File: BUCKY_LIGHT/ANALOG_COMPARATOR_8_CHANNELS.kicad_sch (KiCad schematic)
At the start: 12 parts, among them IC15 LM319N_NOPB, IC16 LM319N_NOPB, IC17 LM319N_NOPB, IC18 LM319N_NOPB

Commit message: finish up robot (i think)
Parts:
- removed IC15, IC16, IC17, IC18: LM319N_NOPB, DIP794W56P254L1905H533Q14N, symbol ANALOG_COMP:LM319N_NOPB
- removed LI21, LI22, LI24, LI25, LI26, LI27 (x2), LI28: LED, symbol Device:LED
- added IC3, IC4: TLV7034RTER, BUCKY_LIGHT:ANALOG_COMP, symbol ANALOG_COMP:TLV7034RTER
- added LI10, LI11, LI12, LI13, LI14, LI8, LI9: LED, LED_SMD:LED_0603_1608Metric, symbol Device:LED
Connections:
- net +5V: now also IC3.2 (VCC), IC4.2 (VCC)
- net GND: now also IC3.11 (VEE), IC4.11 (VEE)
- net I1: now also IC3.1 (+IN_A)
- net I2: now also IC3.4 (+IN_B)
- net I3: now also IC3.9 (+IN_C)
- net I4: now also IC3.12 (+IN_D)
- net I5: now also IC4.1 (+IN_A)
- net I6: now also IC4.4 (+IN_B)
- net I7: now also IC4.9 (+IN_C)
- new net: IC4.15 (OUT_A), LI12.2 (A)
- new net: IC3.14 (OUT_D), LI11.2 (A)
- new net: IC3.15 (OUT_A), LI8.2 (A)
- new net: IC3.6 (OUT_B), LI9.2 (A)
- new net: IC3.7 (OUT_C), LI10.2 (A)
- new net: IC4.6 (OUT_B), LI13.2 (A)
- new net: IC4.7 (OUT_C), LI14.2 (A)
- new net O: LI10.1 (K), LI11.1 (K), LI12.1 (K), LI13.1 (K), LI14.1 (K), LI8.1 (K), LI9.1 (K)
- new net REF_I: IC3.13 (-IN_D), IC3.16 (-IN_A), IC3.5 (-IN_B), IC3.8 (-IN_C), IC4.16 (-IN_A), IC4.5 (-IN_B), IC4.8 (-IN_C)
- no-connect marks 16 -> 6

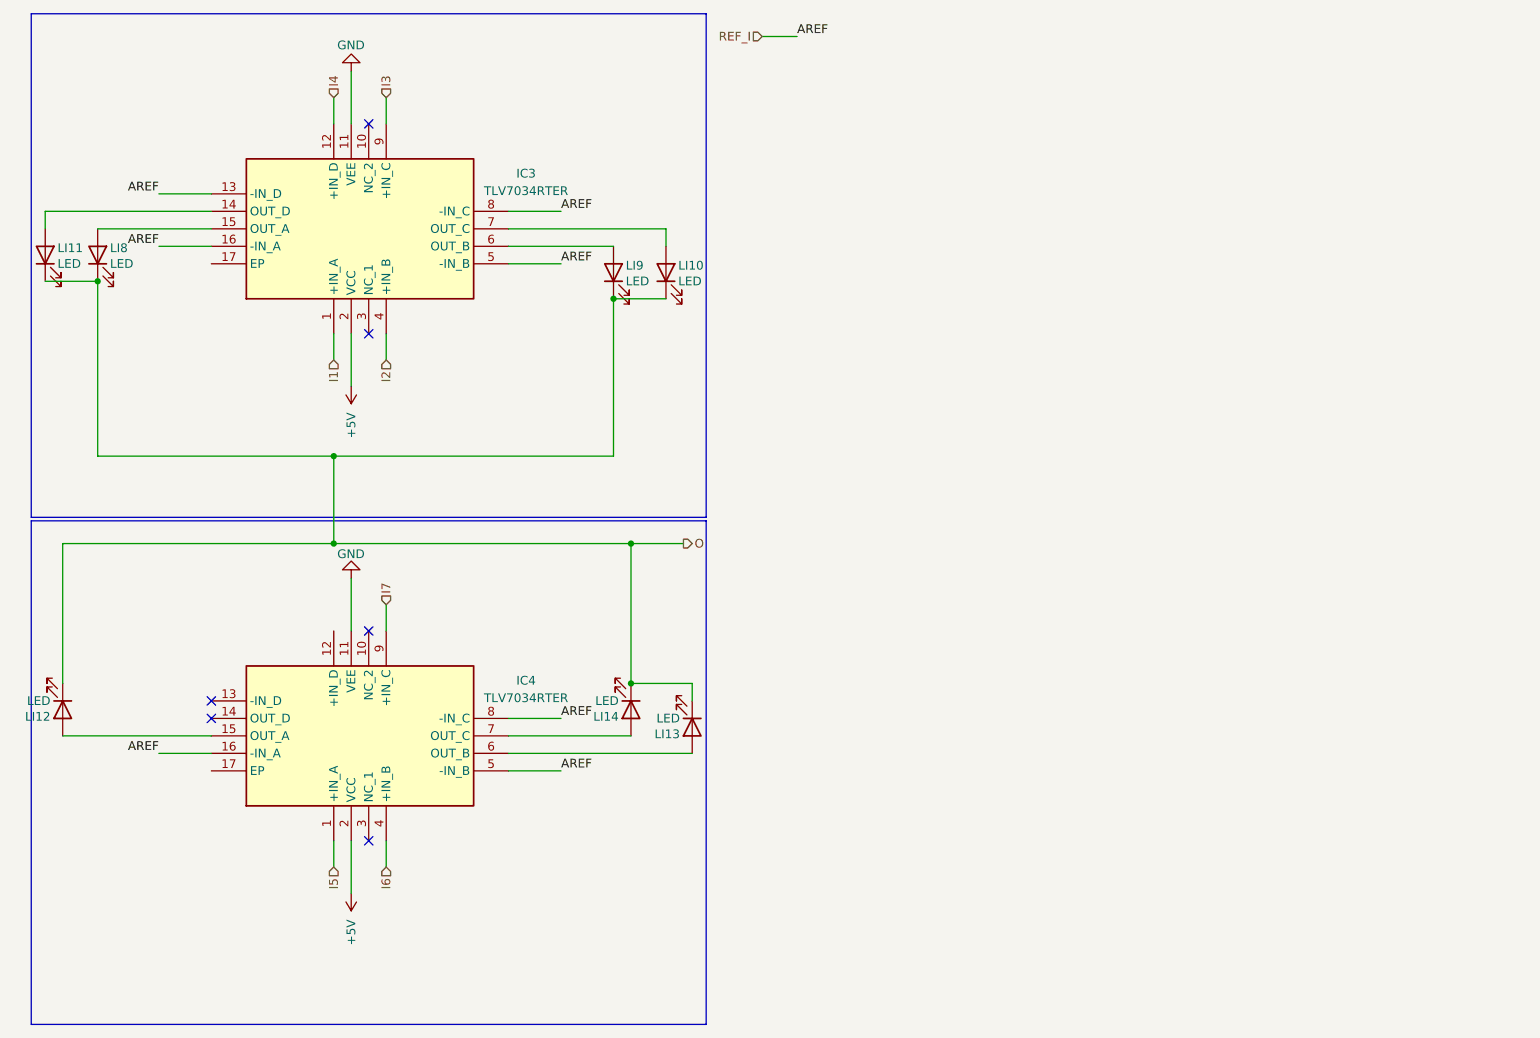
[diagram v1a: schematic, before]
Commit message: chore: convert 2 layer DRIVE -> 4 layer
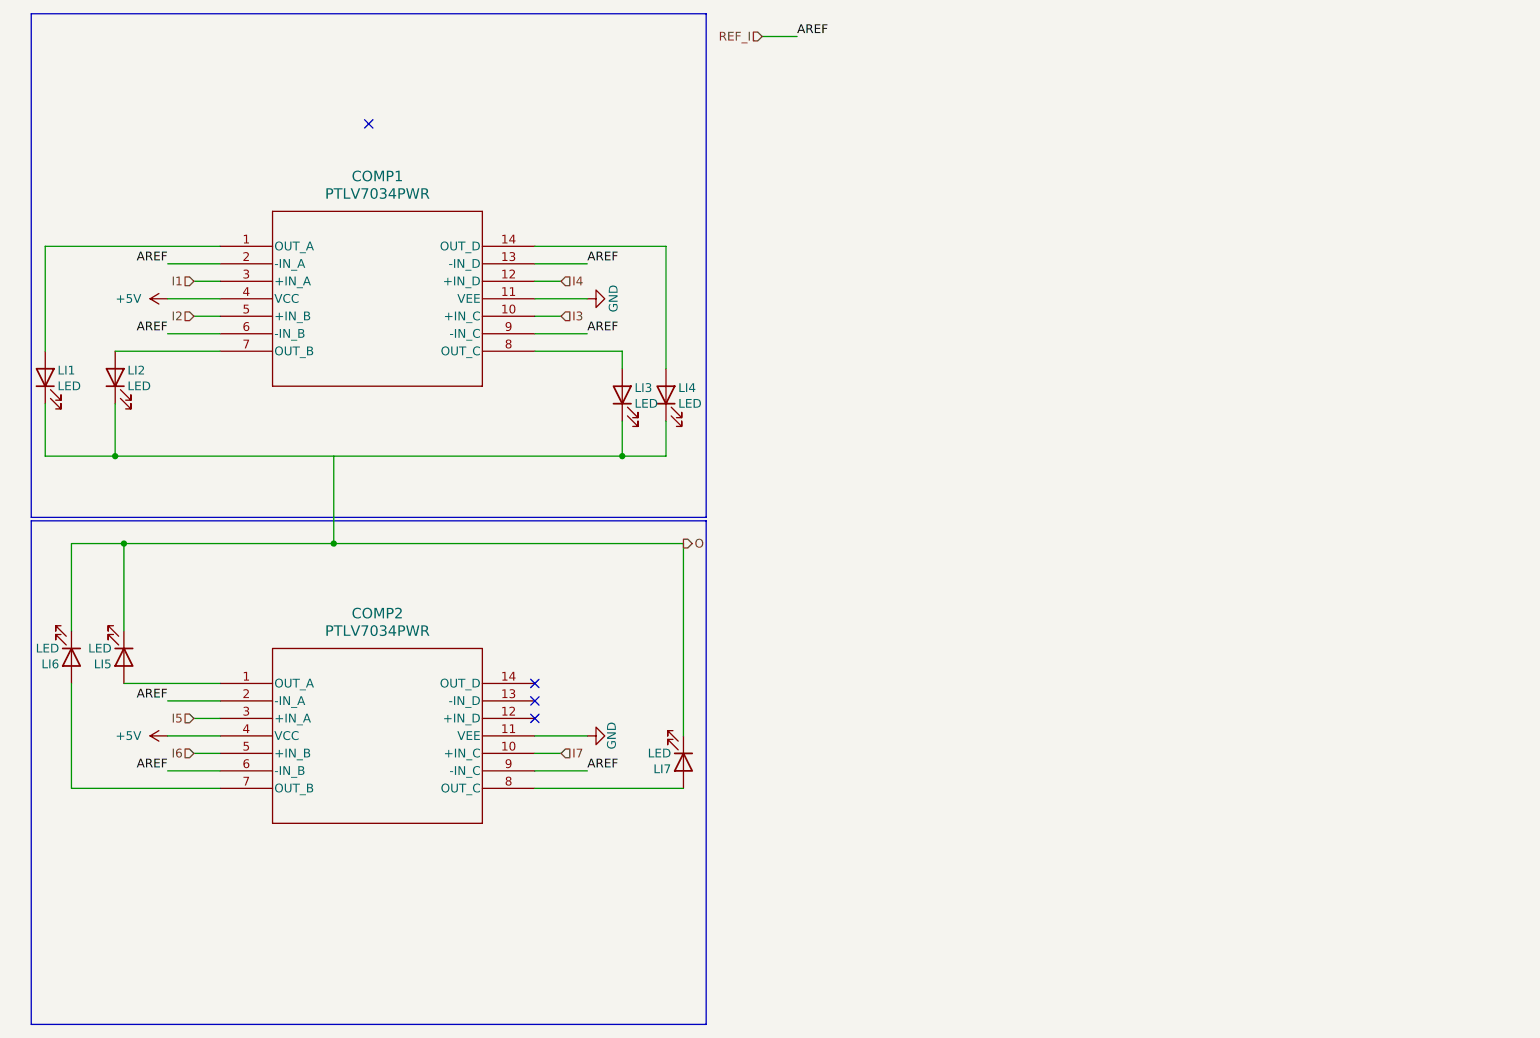
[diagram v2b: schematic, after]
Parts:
- removed IC3, IC4: TLV7034RTER, BUCKY_LIGHT:ANALOG_COMP, symbol ANALOG_COMP:TLV7034RTER
- removed LI10, LI11, LI12, LI13, LI14, LI8, LI9: LED, LED_SMD:LED_0603_1608Metric, symbol Device:LED
- added COMP1, COMP2: PTLV7034PWR, BUCKY_LIGHT:ANALOG_COMP, symbol ANALOG_COMP:PTLV7034PWR
- added LI1, LI2, LI3, LI4, LI5, LI6, LI7: LED, LED_SMD:LED_0603_1608Metric, symbol Device:LED
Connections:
- net +5V: now also COMP1.4 (VCC), COMP2.4 (VCC)
- net GND: now also COMP1.11 (VEE), COMP2.11 (VEE)
- net I1: now also COMP1.3 (+IN_A)
- net I2: now also COMP1.5 (+IN_B)
- net I3: now also COMP1.10 (+IN_C)
- net I4: now also COMP1.12 (+IN_D)
- net I5: now also COMP2.3 (+IN_A)
- net I6: now also COMP2.5 (+IN_B)
- net I7: now also COMP2.10 (+IN_C)
- net O: now also LI5.1 (K), LI6.1 (K), LI7.1 (K)
- net REF_I: now also COMP1.13 (-IN_D), COMP1.2 (-IN_A), COMP1.6 (-IN_B), COMP1.9 (-IN_C), COMP2.2 (-IN_A), COMP2.6 (-IN_B), COMP2.9 (-IN_C)
- new net: COMP1.1 (OUT_A), LI1.2 (A)
- new net: COMP1.14 (OUT_D), LI4.2 (A)
- new net: COMP1.7 (OUT_B), LI2.2 (A)
- new net: COMP1.8 (OUT_C), LI3.2 (A)
- new net: COMP2.8 (OUT_C), LI7.2 (A)
- new net: COMP2.7 (OUT_B), LI6.2 (A)
- new net: LI1.1 (K), LI2.1 (K), LI3.1 (K), LI4.1 (K)
- new net: COMP2.1 (OUT_A), LI5.2 (A)
- no-connect marks 6 -> 4

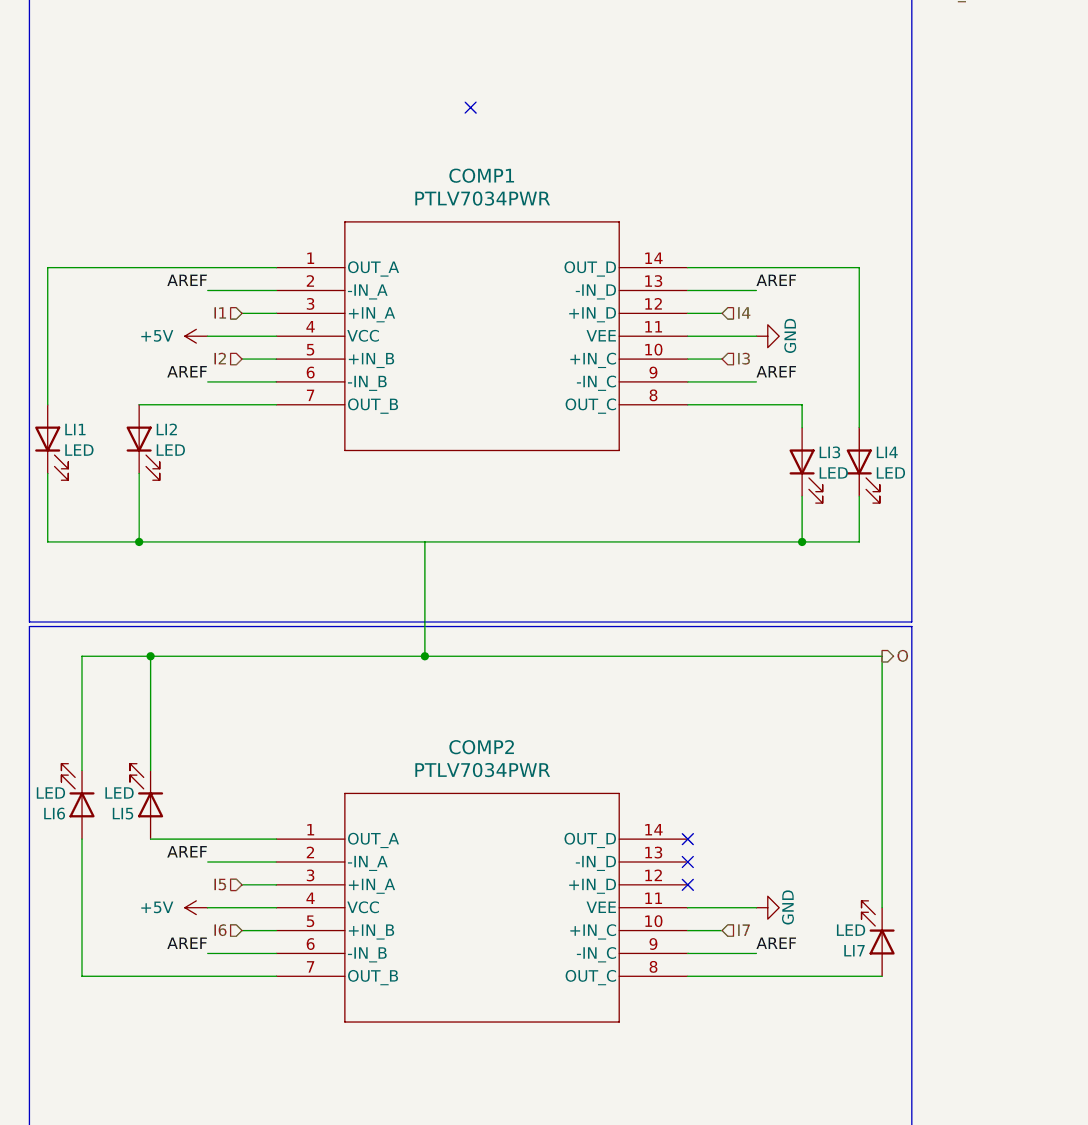
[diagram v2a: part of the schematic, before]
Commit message: chore: make all PCBs from 2 layers to 4 layers
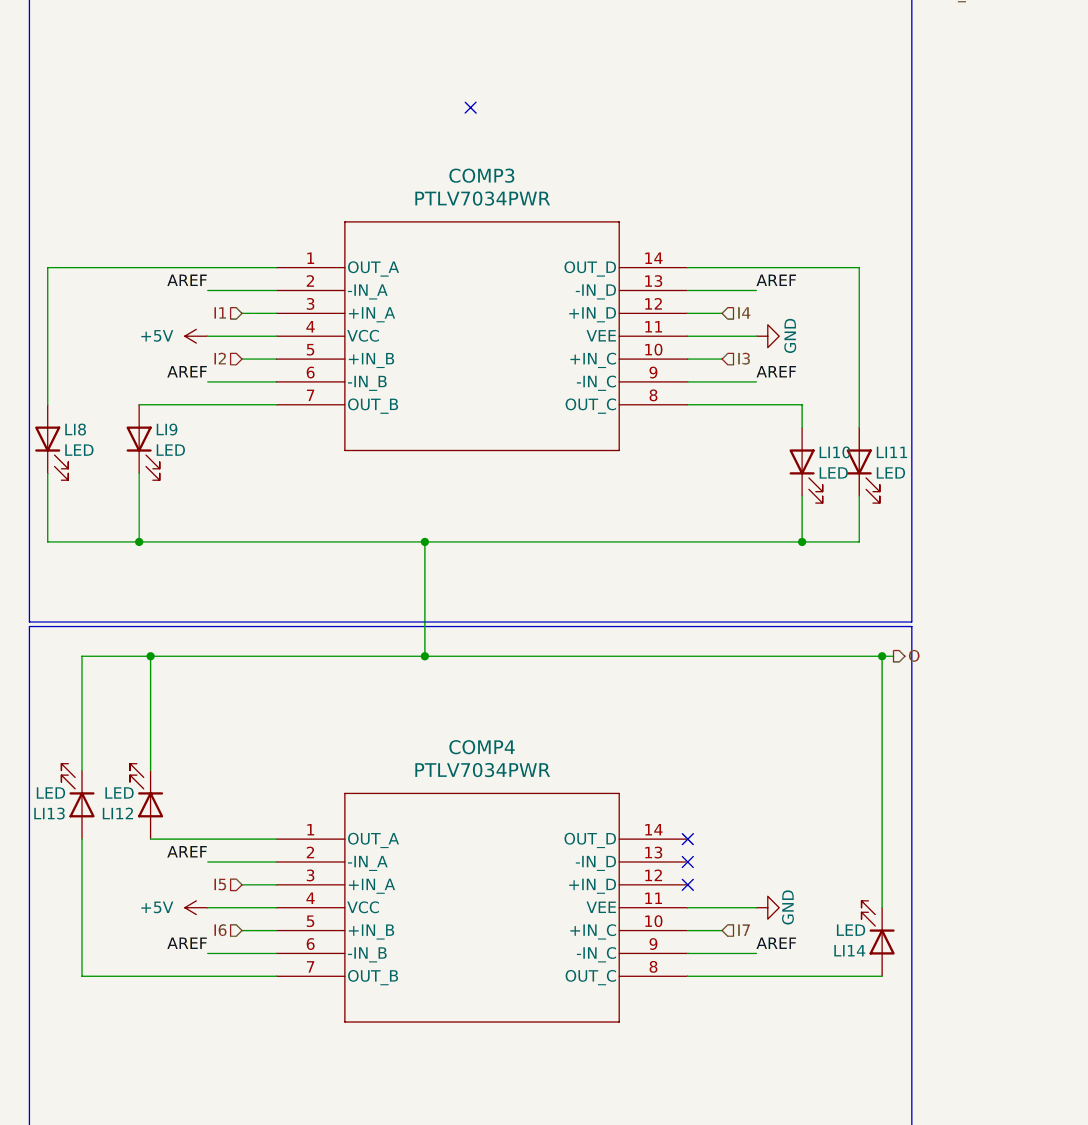
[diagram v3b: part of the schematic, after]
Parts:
- LI10: renamed from LI3; footprint LED_SMD:LED_0603_1608Metric -> LED_SMD:LED_0805_2012Metric
- LI11: renamed from LI4; footprint LED_SMD:LED_0603_1608Metric -> LED_SMD:LED_0805_2012Metric
- LI12: renamed from LI5; footprint LED_SMD:LED_0603_1608Metric -> LED_SMD:LED_0805_2012Metric
- LI13: renamed from LI6; footprint LED_SMD:LED_0603_1608Metric -> LED_SMD:LED_0805_2012Metric
- LI14: renamed from LI7; footprint LED_SMD:LED_0603_1608Metric -> LED_SMD:LED_0805_2012Metric
- LI8: renamed from LI1; footprint LED_SMD:LED_0603_1608Metric -> LED_SMD:LED_0805_2012Metric
- LI9: renamed from LI2; footprint LED_SMD:LED_0603_1608Metric -> LED_SMD:LED_0805_2012Metric
- renumbered COMP1 to COMP3, COMP2 to COMP4
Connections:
- net O: now also LI10.1 (K), LI11.1 (K), LI8.1 (K), LI9.1 (K)
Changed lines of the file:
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@@
 	(title_block
 		(title "BUCKY LIGHT")
-		(date "2024-05-09")
+		(date "2024-09-11")
 		(rev "V1")
 		(company "koen1711")
+	)
+	(junction
+		(at 55.88 76.2)
+		(diameter 0)
+		(color 0 0 0 0)
 	)
 	(junction
@@
 	)
 	(junction
+		(at 106.68 88.9)
+		(diameter 0)
+		(color 0 0 0 0)
+	)
+	(junction
 		(at 24.13 76.2)
 		(diameter 0)
@@
 	(wire
 		(pts
+			(xy 106.68 88.9) (xy 106.68 116.84)
+		)
+		(stroke
+			(width 0)
+			(type default)
+		)
+	)
+	(wire
+		(pts
 			(xy 85.09 124.46) (xy 106.68 124.46)
 		)
@@
 	(wire
 		(pts
-			(xy 106.68 88.9) (xy 106.68 116.84)
-		)
-		(stroke
-			(width 0)
-			(type default)
-		)
-	)
-	(wire
-		(pts
 			(xy 31.75 116.84) (xy 39.37 116.84)
 		)
@@
 	(wire
 		(pts
-			(xy 24.13 76.2) (xy 97.79 76.2)
+			(xy 24.13 76.2) (xy 55.88 76.2)
 		)
 		(stroke
@@
 	(wire
 		(pts
+			(xy 55.88 76.2) (xy 97.79 76.2)
+		)
+		(stroke
+			(width 0)
+			(type default)
+		)
+	)
+	(wire
+		(pts
 			(xy 85.09 116.84) (xy 92.71 116.84)
 		)
@@
 		(pts
 			(xy 25.4 88.9) (xy 55.88 88.9)
+		)
+		(stroke
+			(width 0)
+			(type default)
+		)
+	)
+	(wire
+		(pts
+			(xy 106.68 88.9) (xy 107.95 88.9)
 		)
 		(stroke
@@
 	(hierarchical_label "O"
 		(shape output)
-		(at 106.68 88.9 0)
+		(at 107.95 88.9 0)
 		(fields_autoplaced yes)
 		(effects
@@
 		(dnp no)
 		(fields_autoplaced yes)
-		(property "Reference" "COMP1"
+		(property "Reference" "COMP3"
 			(at 62.23 35.56 0)
 			(effects
@@
 		(dnp no)
 		(fields_autoplaced yes)
-		(property "Reference" "#PWR021"
+		(property "Reference" "#PWR048"
 			(at 35.56 53.34 0)
 			(effects
@@
 		(on_board yes)
 		(dnp no)
-		(property "Reference" "LI7"
+		(property "Reference" "LI14"
 			(at 104.902 121.666 90)
 			(effects
@@
 			)
 		)
-		(property "Footprint" "LED_SMD:LED_0603_1608Metric"
+		(property "Footprint" "LED_SMD:LED_0805_2012Metric"
 			(at 106.68 120.65 0)
 			(effects
@@
 		(on_board yes)
 		(dnp no)
-		(property "Reference" "LI6"
+		(property "Reference" "LI13"
 			(at 16.002 106.426 90)
 			(effects
@@
 			)
 		)
-		(property "Footprint" "LED_SMD:LED_0603_1608Metric"
+		(property "Footprint" "LED_SMD:LED_0805_2012Metric"
 			(at 17.78 105.41 0)
 			(effects
@@
 		(on_board yes)
 		(dnp no)
-		(property "Reference" "LI2"
+		(property "Reference" "LI9"
 			(at 25.908 63.754 90)
 			(effects
@@
 			)
 		)
-		(property "Footprint" "LED_SMD:LED_0603_1608Metric"
+		(property "Footprint" "LED_SMD:LED_0805_2012Metric"
 			(at 24.13 64.77 0)
 			(effects
@@
 		(on_board yes)
 		(dnp no)
-		(property "Reference" "LI1"
+		(property "Reference" "LI8"
 			(at 15.748 63.754 90)
 			(effects
@@
 			)
 		)
-		(property "Footprint" "LED_SMD:LED_0603_1608Metric"
+		(property "Footprint" "LED_SMD:LED_0805_2012Metric"
 			(at 13.97 64.77 0)
 			(effects
@@
 		(on_board yes)
 		(dnp no)
-		(property "Reference" "LI4"
+		(property "Reference" "LI11"
 			(at 105.918 66.294 90)
 			(effects
@@
 			)
 		)
-		(property "Footprint" "LED_SMD:LED_0603_1608Metric"
+		(property "Footprint" "LED_SMD:LED_0805_2012Metric"
 			(at 104.14 67.31 0)
 			(effects
@@
 		(dnp no)
 		(fields_autoplaced yes)
-		(property "Reference" "#PWR018"
+		(property "Reference" "#PWR023"
 			(at 35.56 116.84 0)
 			(effects
@@
 		(on_board yes)
 		(dnp no)
-		(property "Reference" "LI5"
+		(property "Reference" "LI12"
 			(at 23.622 106.426 90)
 			(effects
@@
 			)
 		)
-		(property "Footprint" "LED_SMD:LED_0603_1608Metric"
+		(property "Footprint" "LED_SMD:LED_0805_2012Metric"
 			(at 25.4 105.41 0)
 			(effects
@@
 		(dnp no)
 		(fields_autoplaced yes)
-		(property "Reference" "COMP2"
+		(property "Reference" "COMP4"
 			(at 62.23 99.06 0)
 			(effects
@@
 		(on_board yes)
 		(dnp no)
-		(property "Reference" "#PWR020"
+		(property "Reference" "#PWR047"
 			(at 99.06 53.34 0)
 			(effects
@@
 		(on_board yes)
 		(dnp no)
-		(property "Reference" "#PWR022"
+		(property "Reference" "#PWR042"
 			(at 99.06 116.84 0)
 			(effects
@@
 		(on_board yes)
 		(dnp no)
-		(property "Reference" "LI3"
+		(property "Reference" "LI10"
 			(at 99.568 66.294 90)
 			(effects
@@
 			)
 		)
-		(property "Footprint" "LED_SMD:LED_0603_1608Metric"
+		(property "Footprint" "LED_SMD:LED_0805_2012Metric"
 			(at 97.79 67.31 0)
 			(effects
